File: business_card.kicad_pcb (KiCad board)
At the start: 2 copper layers, 88.9 x 50.8 mm, 14 parts, among them Q1 2N3904, SW1 DS01-254-S-01BE, U1 TLC555IP

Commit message: Update PCB layout
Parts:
- moved R2 20.5 mm to (191.0, 114.1), turned to 90 degrees
- moved RV1 15.0 mm to (188.0, 121.5), turned to -90 degrees
- moved C2 11.9 mm to (175.0, 119.5), turned to -90 degrees
- moved C1 10.5 mm to (179.0, 111.0), turned to -90 degrees
- moved R3 8.67 mm to (150.1, 106.0), turned to 180 degrees
- moved D2 7.50 mm to (164.0, 125.5)
- moved D1 6.02 mm to (155.0, 125.5)
- moved Q1 4.53 mm to (133.0, 112.3)
- moved SW1 2.65 mm to (134.0, 125.0)
- moved R1 2.50 mm to (172.9, 105.0)
- moved R4 1.58 mm to (139.9, 111.0)
- moved R5 1.58 mm to (139.9, 116.0)
- moved BT1 0.74 mm to (119.5, 114.9)
- moved U1 0.58 mm to (161.0, 110.8)
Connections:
- SW1 pad 1: Net-(BT1-+) -> +3V0
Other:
- outline, holes or cut-outs redrawn

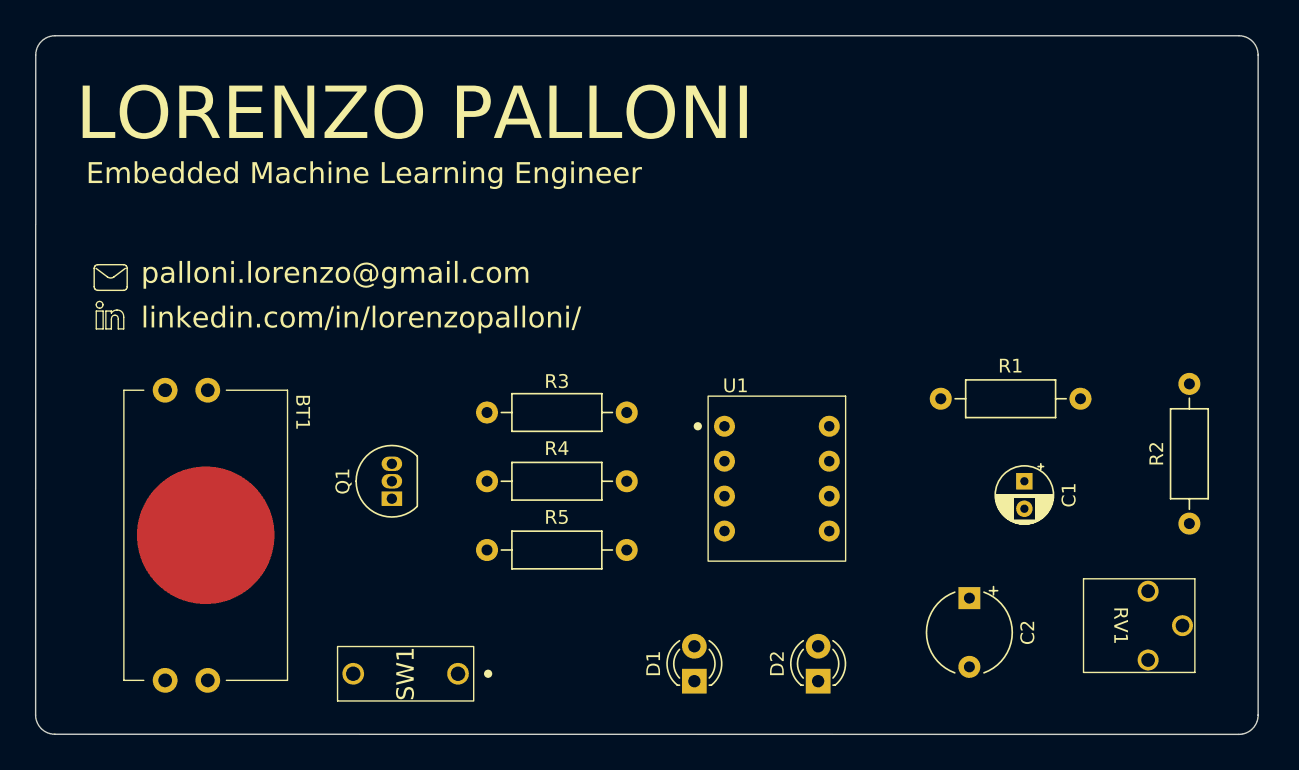
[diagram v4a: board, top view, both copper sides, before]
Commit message: Add traces and Replace 2N3904 footprint
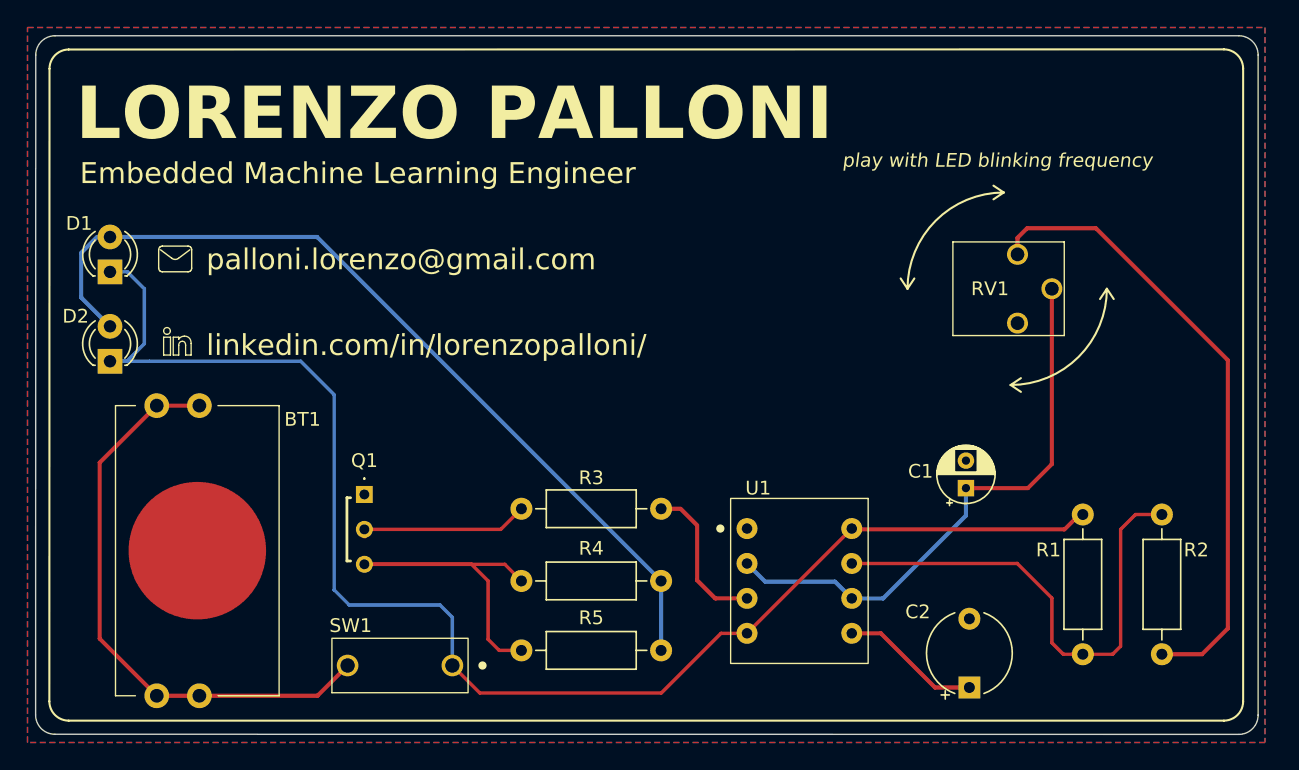
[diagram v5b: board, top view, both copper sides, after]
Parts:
- Q1: footprint Package_TO_SOT_THT:TO-92_Inline -> business_card:2N3904
- moved D2 56.5 mm to (112.5, 102.3)
- moved D1 51.9 mm to (112.5, 95.8)
- moved RV1 26.3 mm to (178.5, 97.0)
- moved R1 13.3 mm to (183.2, 113.4), turned to -90 degrees
- moved R2 9.71 mm to (189.0, 123.6)
- moved R5 7.72 mm to (142.4, 123.3)
- moved R4 7.67 mm to (142.4, 118.2)
- moved U1 7.62 mm to (162.6, 118.2)
- moved R3 7.43 mm to (152.6, 113.0)
- moved C2 6.50 mm to (175.0, 126.0), turned to 90 degrees
- moved C1 4.28 mm to (174.8, 111.5), turned to 90 degrees
- moved Q1 2.02 mm to (131.0, 112.0), turned to -90 degrees
- moved BT1 1.28 mm to (118.8, 116.0)
- moved SW1 0.73 mm to (133.6, 124.4)
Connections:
- BT1 pad 1: +3V0 -> GND
- BT1 pad 5: GND -> +3V0
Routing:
- net +3V0: track 0.00 -> 149.1 mm
- net Net-(D1-A): track 0.00 -> 64.0 mm
- net Net-(R2-Pad1): track 0.00 -> 45.6 mm
- net /THRES/TRIG: track 0.00 -> 40.7 mm
- net /DISCH: track 0.00 -> 36.8 mm
- net Net-(Q1-C): track 0.00 -> 28.7 mm
- net Net-(Q1-B): track 0.00 -> 12.3 mm
- net /OUT: track 0.00 -> 11.6 mm
- net /CONT: track 0.00 -> 9.68 mm
- added copper zone on B.Cu, net GND
- added copper zone on F.Cu, net GND
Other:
- board text added: "play with LED blinking frequency"

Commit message: Add license and 2n3904 3d model
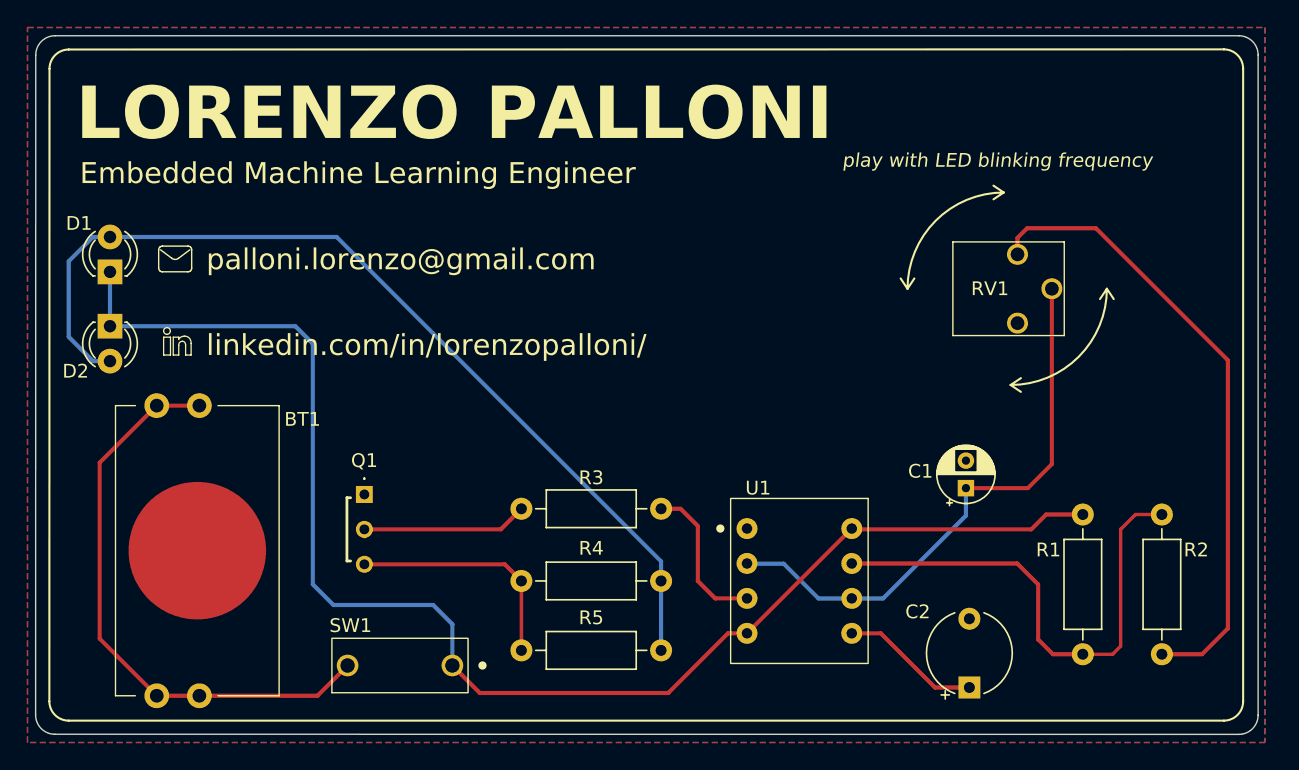
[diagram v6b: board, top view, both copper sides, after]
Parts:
- moved D2 2.55 mm to (112.5, 99.7), turned to -90 degrees
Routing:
- net Net-(Q1-C): track 28.7 -> 17.3 mm
- net Net-(D1-A): track 64.0 -> 69.3 mm
- net +3V0: track 149.1 -> 145.9 mm
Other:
- board text added: "business card v01"

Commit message: Make the board ready for manufacturing! :)
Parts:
- turned SW1 to -90 degrees
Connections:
- BT1 pad 2: +3V0 -> Net-(BT1-+3V0-Pad2)
- BT1 pad 3: +3V0 -> Net-(BT1-+3V0-Pad2)
- BT1 pad 4: +3V0 -> Net-(BT1-+3V0-Pad2)
- BT1 pad 5: +3V0 -> Net-(BT1-+3V0-Pad2)
- SW1 pad 1: +3V0 -> Net-(BT1-+3V0-Pad2)
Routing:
- net +3V0: track 145.9 -> 103.6 mm
- net Net-(BT1-+3V0-Pad2): track 0.00 -> 42.3 mm
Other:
- board text added: "OFF"
- board text added: "ON"
